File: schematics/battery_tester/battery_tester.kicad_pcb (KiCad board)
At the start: 2 copper layers, 170 x 155 mm, 39 parts, among them J1 BATT1, J101 XIAO_LEFT, J102 XIAO_RIGHT, J103 ADS1115_1, J104 ADS1115_2, J105 LED_STRIP, J2 BATT2, J3 BATT3, J4 BATT4, J5 BATT5, J6 BATT6, J7 BATT7, J8 BATT8, Q1 IRLZ44N, Q2 IRLZ44N, Q3 IRLZ44N, Q4 IRLZ44N, Q5 IRLZ44N, Q6 IRLZ44N, Q7 IRLZ44N, Q8 IRLZ44N

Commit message: Add v1.0.0 PCB layout with routed board and gerber outputs
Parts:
- moved J101 82.5 mm to (91.5, 29.9)
- moved J102 82.5 mm to (109.0, 29.9)
- moved R10 77.3 mm to (124.5, 33.0), turned to -90 degrees
- moved R15 64.7 mm to (36.5, 83.0)
- moved R16 64.7 mm to (74.5, 83.0)
- moved R17 64.7 mm to (112.5, 83.0)
- moved R18 64.7 mm to (150.5, 83.0)
- moved Q5 57.8 mm to (55.5, 83.0), turned to -90 degrees
- moved Q6 57.8 mm to (93.5, 83.0), turned to -90 degrees
- moved Q7 57.8 mm to (131.5, 83.0), turned to -90 degrees
- moved Q8 57.8 mm to (169.5, 83.0), turned to -90 degrees
- moved J104 52.2 mm to (136.3, 45.5), turned to 90 degrees
- moved J103 48.8 mm to (40.2, 45.0), turned to 90 degrees
- moved J105 45.2 mm to (169.5, 29.9)
- moved R11 37.8 mm to (36.5, 61.0)
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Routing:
- net GND: track 0.00 -> 691.6 mm
- net GPIO9: track 0.00 -> 234.3 mm
- net GPIO8: track 0.00 -> 195.6 mm
- net GPIO10: track 0.00 -> 175.2 mm
- net BATT5+: track 0.00 -> 154.7 mm
- net +3V3: track 0.00 -> 126.4 mm, vias 0 -> 2
- net SDA: track 0.00 -> 120.9 mm, vias 0 -> 1
- net BATT4+: track 0.00 -> 120.5 mm
- net SCL: track 0.00 -> 119.9 mm, vias 0 -> 2
- net BATT6+: track 0.00 -> 118.9 mm
- net GPIO20: track 0.00 -> 117.2 mm
- net GPIO5: track 0.00 -> 96.6 mm
- net BATT7+: track 0.00 -> 90.9 mm
- net BATT3+: track 0.00 -> 85.0 mm
- net BATT8+: track 0.00 -> 84.6 mm
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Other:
- board size 170 x 155 mm -> 155.5 x 82.5 mm
- board text added: "Battery Tester V1.0.0"
- board text removed: "CONTROL"

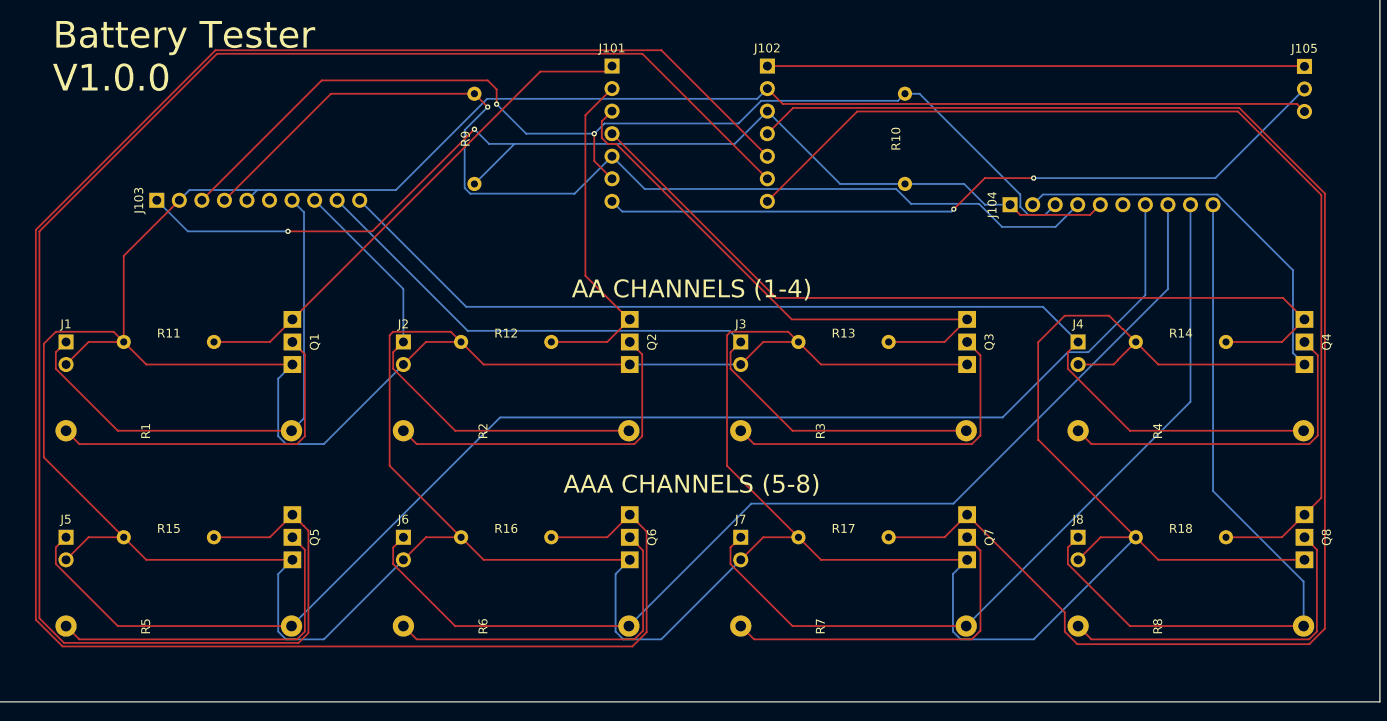
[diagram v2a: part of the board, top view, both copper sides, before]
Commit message: Add ADC test utility and update PCB layout
Introduces a new binary to validate battery voltage readings via I2C
and updates the hardware schematics for the battery tester.
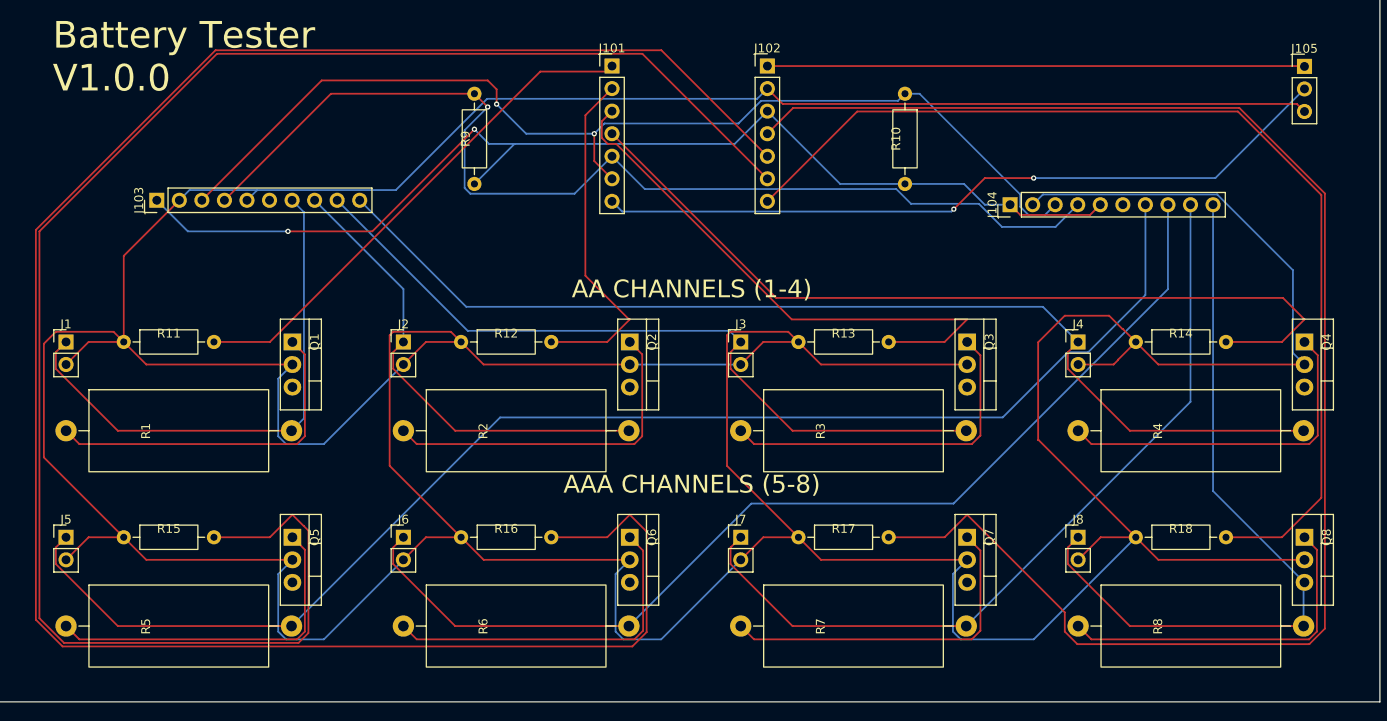
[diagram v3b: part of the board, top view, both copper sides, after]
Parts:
- R1, R2, R3, R4, R5, R6, R7, R8: footprint Resistor_THT:R_Axial_DIN0922_L20.3mm_D9.9mm_P25.40mm_Horizontal -> Resistor_THT:R_Axial_DIN0922_L20.0mm_D9.0mm_P25.40mm_Horizontal

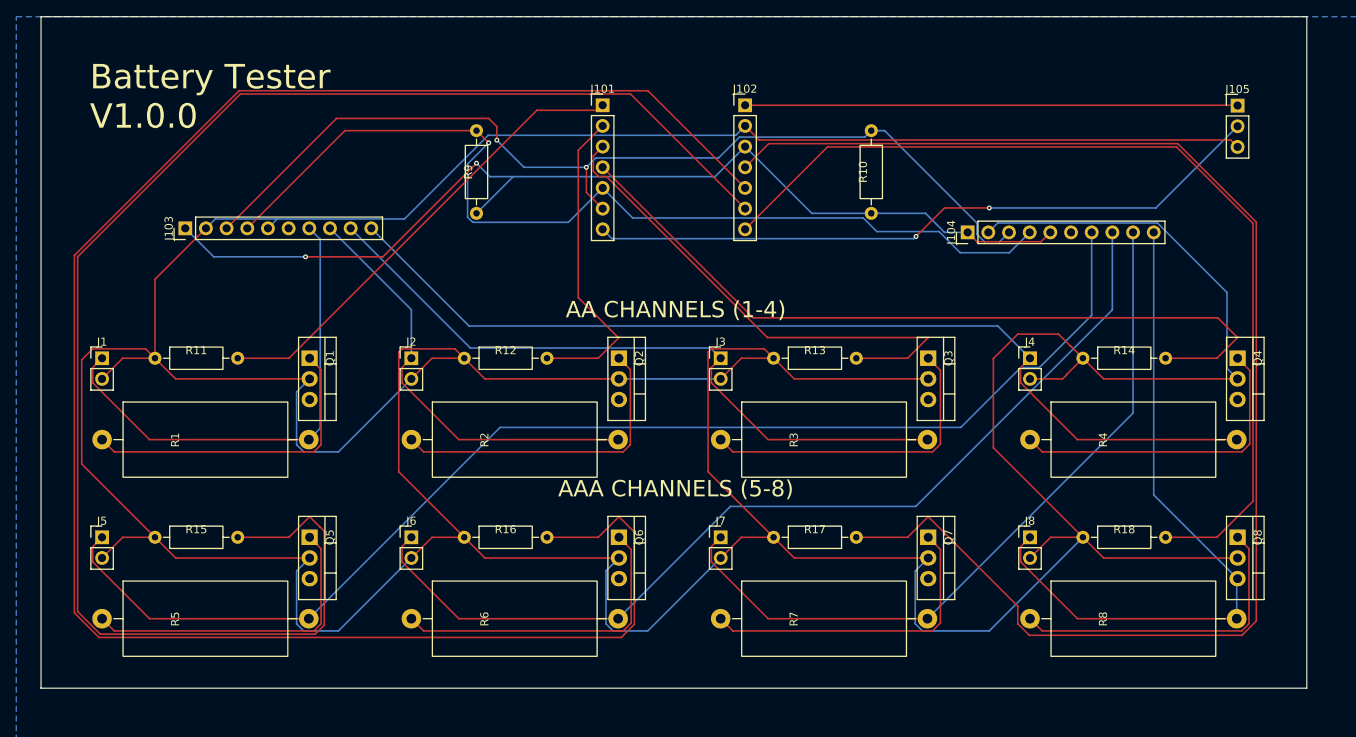
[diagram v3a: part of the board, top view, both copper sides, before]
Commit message: Update battery tester hardware and LED logic
Major revision to KiCad schematics and PCB layout (v2.0). Refines LED
behavior by reducing brightness, removing flashing for weak batteries in
favor of a solid color, and wrapping LED writes in a critical section.
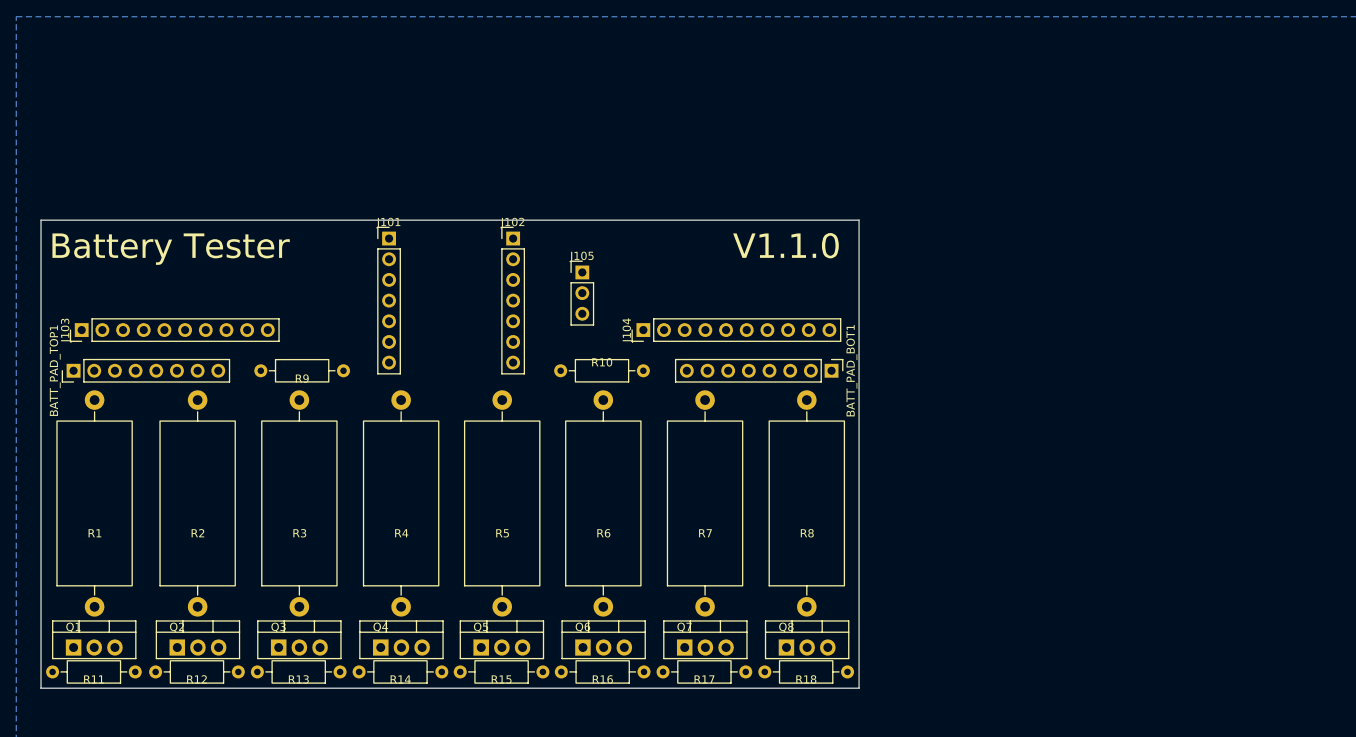
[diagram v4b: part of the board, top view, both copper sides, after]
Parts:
- removed J1: BATT1, Connector_PinHeader_2.54mm:PinHeader_1x02_P2.54mm_Vertical
- removed J2: BATT2, Connector_PinHeader_2.54mm:PinHeader_1x02_P2.54mm_Vertical
- removed J3: BATT3, Connector_PinHeader_2.54mm:PinHeader_1x02_P2.54mm_Vertical
- removed J4: BATT4, Connector_PinHeader_2.54mm:PinHeader_1x02_P2.54mm_Vertical
- removed J5: BATT5, Connector_PinHeader_2.54mm:PinHeader_1x02_P2.54mm_Vertical
- removed J6: BATT6, Connector_PinHeader_2.54mm:PinHeader_1x02_P2.54mm_Vertical
- removed J7: BATT7, Connector_PinHeader_2.54mm:PinHeader_1x02_P2.54mm_Vertical
- removed J8: BATT8, Connector_PinHeader_2.54mm:PinHeader_1x02_P2.54mm_Vertical
- added BATT_PAD_BOT1: Conn_01x08, Connector_PinHeader_2.54mm:PinHeader_1x08_P2.54mm_Vertical, F.Cu at (119.6, 62.5)
- added BATT_PAD_TOP1: Conn_01x08, Connector_PinHeader_2.54mm:PinHeader_1x08_P2.54mm_Vertical, F.Cu at (26.5, 62.5)
- R1, R2, R3, R4, R5, R6, R7, R8: value 2.2R_5W -> 2.2R 5W
- moved Q4 111.1 mm to (64.2, 96.5), turned to 0 degrees
- moved R14 87.7 mm to (71.7, 99.5), turned to 180 degrees
- moved Q3 87.4 mm to (51.7, 96.5), turned to 0 degrees
- moved J105 83.1 mm to (89.0, 50.4)
- moved R4 79.9 mm to (66.7, 91.5), turned to 90 degrees
- moved R13 65.7 mm to (59.2, 99.5), turned to 180 degrees
- moved Q2 64.9 mm to (39.2, 96.5), turned to 0 degrees
- moved Q8 57.1 mm to (114.1, 96.5), turned to 0 degrees
- moved R3 55.7 mm to (54.2, 91.5), turned to 90 degrees
- moved R15 50.4 mm to (84.2, 99.5), turned to 180 degrees
- moved R5 49.2 mm to (79.2, 91.5), turned to 90 degrees
- moved R12 47.5 mm to (46.7, 99.5), turned to 180 degrees
- moved Q1 45.9 mm to (26.5, 96.5), turned to 0 degrees
- moved J104 41.6 mm to (96.5, 57.5)
- moved R10 40.7 mm to (96.5, 62.5), turned to 180 degrees
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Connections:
- net CH1_D renamed /CH1_D
- net CH2_D renamed /CH2_D
- net CH3_D renamed /CH3_D
- net CH4_D renamed /CH4_D
- net CH5_D renamed /CH5_D
- net CH6_D renamed /CH6_D
- net CH7_D renamed /CH7_D
- net CH8_D renamed /CH8_D
- J101 pad 1: GPIO2 -> unconnected-(J101-Pin_1-Pad1)
- J101 pad 2: GPIO3 -> unconnected-(J101-Pin_2-Pad2)
- J101 pad 3: GPIO4 -> unconnected-(J101-Pin_3-Pad3)
- J101 pad 4: GPIO5 -> unconnected-(J101-Pin_4-Pad4)
- J101 pad 5: SDA -> unconnected-(J101-Pin_5-Pad5)
- J101 pad 6: SCL -> unconnected-(J101-Pin_6-Pad6)
- J101 pad 7: LED_DATA -> unconnected-(J101-Pin_7-Pad7)
- J102 pad 1: +5V -> unconnected-(J102-Pin_1-Pad1)
- J102 pad 2: GND -> unconnected-(J102-Pin_2-Pad2)
- J102 pad 3: +3V3 -> unconnected-(J102-Pin_3-Pad3)
- J102 pad 4: GPIO10 -> unconnected-(J102-Pin_4-Pad4)
- J102 pad 5: GPIO9 -> unconnected-(J102-Pin_5-Pad5)
- J102 pad 6: GPIO8 -> unconnected-(J102-Pin_6-Pad6)
- J102 pad 7: GPIO20 -> unconnected-(J102-Pin_7-Pad7)
- J103 pad 1: +3V3 -> unconnected-(J103-Pin_1-Pad1)
- J103 pad 10: BATT4+ -> unconnected-(J103-Pin_10-Pad10)
- J103 pad 2: GND -> unconnected-(J103-Pin_2-Pad2)
- J103 pad 3: SCL -> unconnected-(J103-Pin_3-Pad3)
- J103 pad 4: SDA -> unconnected-(J103-Pin_4-Pad4)
- J103 pad 5: GND -> unconnected-(J103-Pin_5-Pad5)
- J103 pad 6: (no net) -> unconnected-(J103-Pin_6-Pad6)
- J103 pad 7: BATT1+ -> unconnected-(J103-Pin_7-Pad7)
- J103 pad 8: BATT2+ -> unconnected-(J103-Pin_8-Pad8)
- J103 pad 9: BATT3+ -> unconnected-(J103-Pin_9-Pad9)
- J104 pad 1: +3V3 -> unconnected-(J104-Pin_1-Pad1)
- J104 pad 10: BATT8+ -> unconnected-(J104-Pin_10-Pad10)
- J104 pad 2: GND -> unconnected-(J104-Pin_2-Pad2)
- J104 pad 3: SCL -> unconnected-(J104-Pin_3-Pad3)
- J104 pad 4: SDA -> unconnected-(J104-Pin_4-Pad4)
- J104 pad 5: +3V3 -> unconnected-(J104-Pin_5-Pad5)
- J104 pad 6: (no net) -> unconnected-(J104-Pin_6-Pad6)
- J104 pad 7: BATT5+ -> unconnected-(J104-Pin_7-Pad7)
- J104 pad 8: BATT6+ -> unconnected-(J104-Pin_8-Pad8)
- J104 pad 9: BATT7+ -> unconnected-(J104-Pin_9-Pad9)
- J105 pad 1: +5V -> unconnected-(J105-Pin_1-Pad1)
- J105 pad 2: LED_DATA -> unconnected-(J105-Pin_2-Pad2)
- J105 pad 3: GND -> unconnected-(J105-Pin_3-Pad3)
- Q1 pad 1: GPIO2 -> /GPIO2
- Q1 pad 3: GND -> /GND
- Q2 pad 1: GPIO3 -> /GPIO3
- Q2 pad 3: GND -> /GND
- Q3 pad 1: GPIO4 -> /GPIO4
- Q3 pad 3: GND -> /GND
- Q4 pad 1: GPIO5 -> /GPIO5
- Q4 pad 3: GND -> /GND
- Q5 pad 1: GPIO8 -> /GPIO8
- Q5 pad 3: GND -> /GND
- Q6 pad 1: GPIO9 -> /GPIO9
- Q6 pad 3: GND -> /GND
- Q7 pad 1: GPIO10 -> /GPIO10
- Q7 pad 3: GND -> /GND
- Q8 pad 1: GPIO20 -> /GPIO20
- Q8 pad 3: GND -> /GND
- R1 pad 2: BATT1+ -> /BATT1+
- R10 pad 1: SCL -> /SCL
- R10 pad 2: +3V3 -> /+3V3
- R11 pad 1: GND -> /GND
- R11 pad 2: GPIO2 -> /GPIO2
- R12 pad 1: GND -> /GND
- R12 pad 2: GPIO3 -> /GPIO3
- R13 pad 1: GND -> /GND
- R13 pad 2: GPIO4 -> /GPIO4
- R14 pad 1: GND -> /GND
- R14 pad 2: GPIO5 -> /GPIO5
- R15 pad 1: GND -> /GND
- R15 pad 2: GPIO8 -> /GPIO8
- R16 pad 1: GND -> /GND
- R16 pad 2: GPIO9 -> /GPIO9
- R17 pad 1: GND -> /GND
- R17 pad 2: GPIO10 -> /GPIO10
- R18 pad 1: GND -> /GND
- R18 pad 2: GPIO20 -> /GPIO20
- R2 pad 2: BATT2+ -> /BATT2+
- R3 pad 2: BATT3+ -> /BATT3+
- R4 pad 2: BATT4+ -> /BATT4+
- R5 pad 2: BATT5+ -> /BATT5+
- R6 pad 2: BATT6+ -> /BATT6+
- R7 pad 2: BATT7+ -> /BATT7+
- R8 pad 2: BATT8+ -> /BATT8+
- R9 pad 1: SDA -> /SDA
- R9 pad 2: +3V3 -> /+3V3
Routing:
- net GND: track 691.6 -> 0.00 mm
- net GPIO9: track 234.3 -> 0.00 mm
- net GPIO8: track 195.6 -> 0.00 mm
- net GPIO10: track 175.2 -> 0.00 mm
- net BATT5+: track 154.7 -> 0.00 mm
- net +3V3: track 126.4 -> 0.00 mm, vias 2 -> 0
- net SDA: track 120.9 -> 0.00 mm, vias 1 -> 0
- net BATT4+: track 120.5 -> 0.00 mm
- net SCL: track 119.9 -> 0.00 mm, vias 2 -> 0
- net BATT6+: track 118.9 -> 0.00 mm
- net GPIO20: track 117.2 -> 0.00 mm
- net GPIO5: track 96.6 -> 0.00 mm
- net BATT7+: track 90.9 -> 0.00 mm
- net BATT3+: track 85.0 -> 0.00 mm
- net BATT8+: track 84.6 -> 0.00 mm
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- added copper zone on B.Cu, net /GND
- removed copper zone on B.Cu, net GND
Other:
- board size 155.5 x 82.5 mm -> 100.5 x 57.5 mm
- board text added: "Battery Tester"
- board text added: "V1.1.0"
- board text removed: "AA CHANNELS (1-4)"
- board text removed: "AAA CHANNELS (5-8)"
- board text removed: "Battery Tester V1.0.0"
